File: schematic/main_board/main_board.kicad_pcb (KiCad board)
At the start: 2 copper layers, 15 parts, among them J1 Line OUT, J2 Line IN, P1 +Vref, P2 GND, P3 -Vref, P4 Probe, P5 GND, U1 LM324N

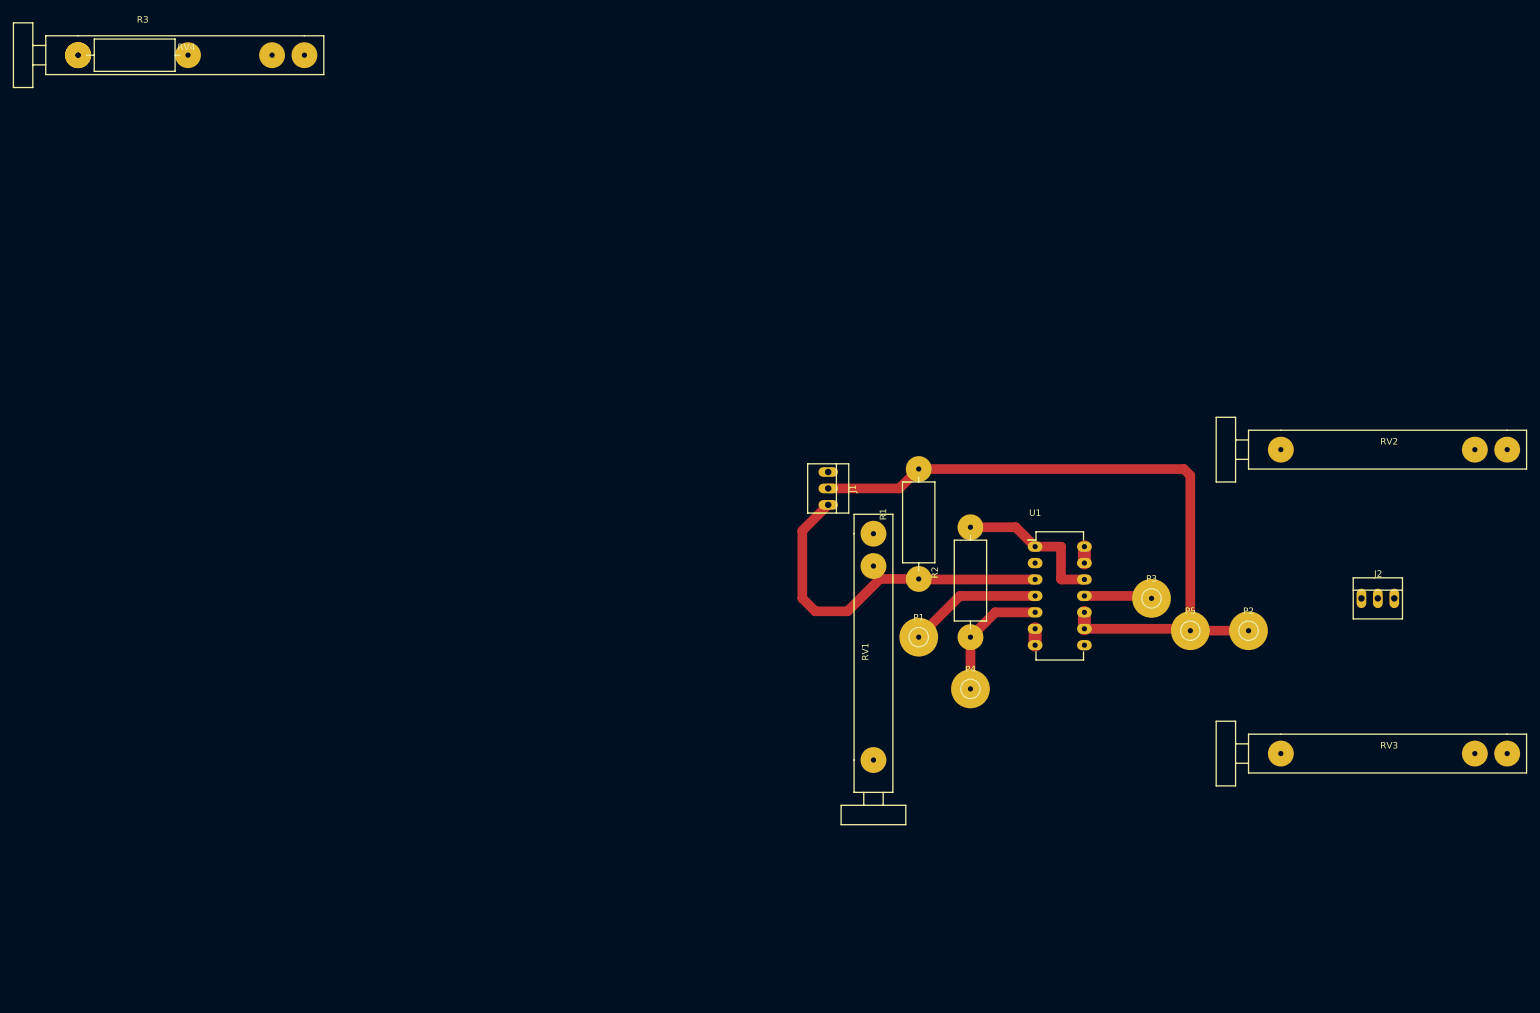
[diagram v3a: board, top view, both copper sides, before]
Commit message: Added footprints for some soviet elements which used on Main board.
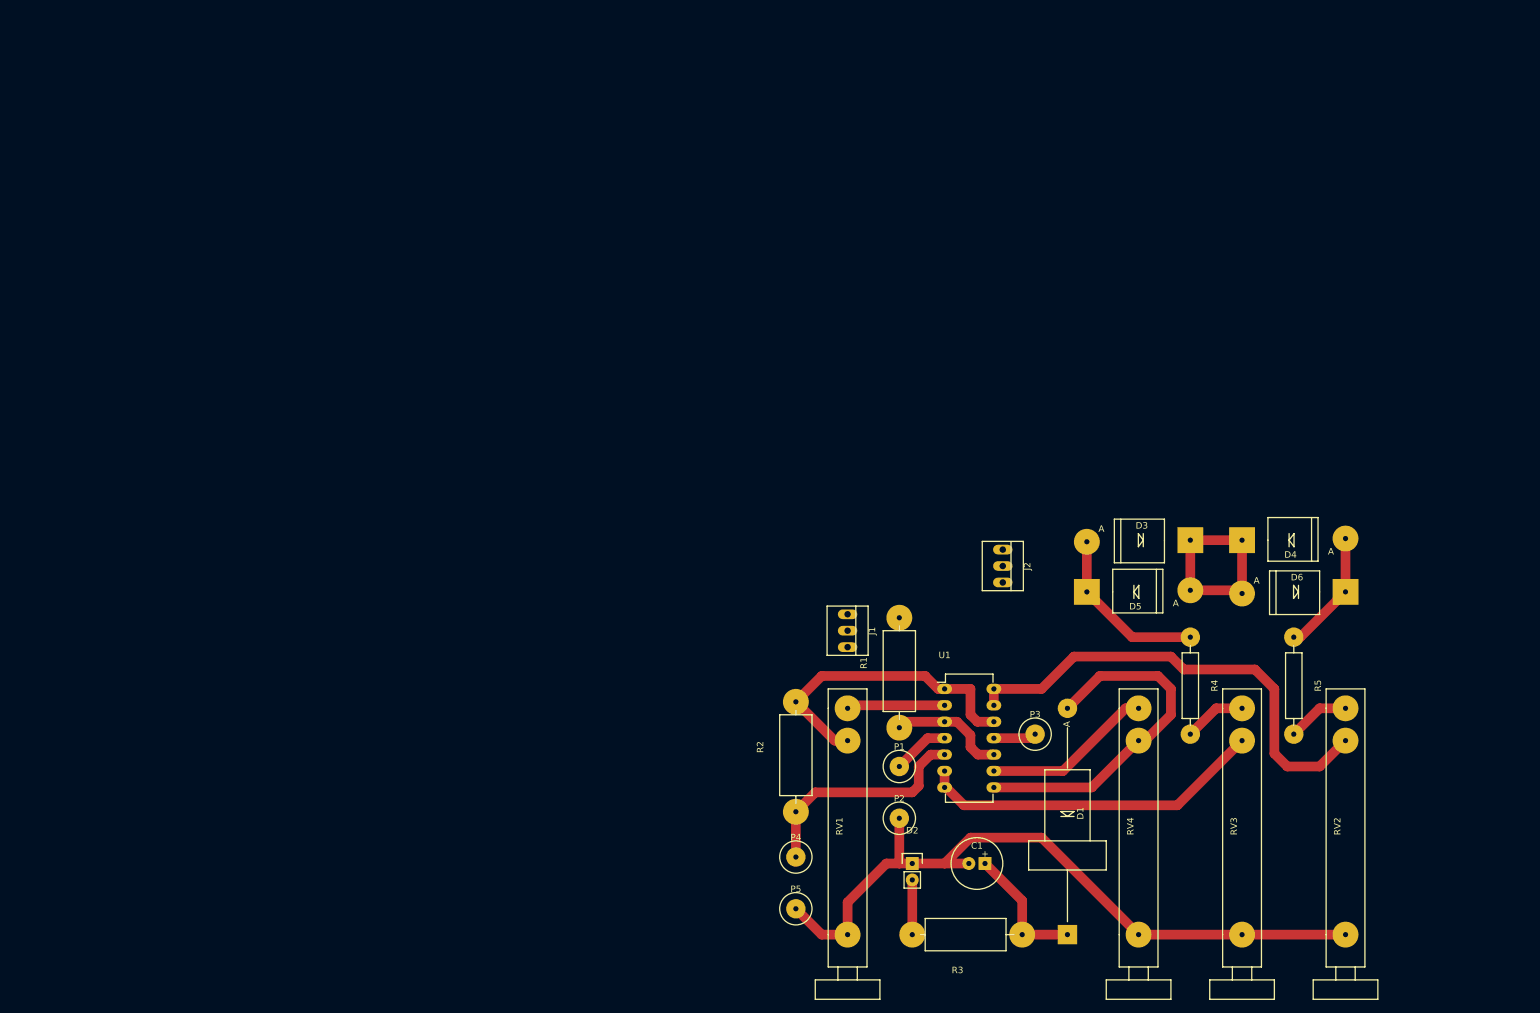
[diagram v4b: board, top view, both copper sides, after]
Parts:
- added C1: 100u, footprints:C100u_vert, F.Cu at (139.0, 125.0)
- added D1: D226, footprints:Diode_D226, F.Cu at (153.0, 136.0)
- added D2: LED, footprints:Pin_vert_1x02, F.Cu at (129.0, 125.0)
- added D3: KD105, footprints:Diode_KD105, F.Cu at (172.0, 75.0)
- added D4: KD105, footprints:Diode_KD105, F.Cu at (180.0, 75.0)
- added D5: KD105, footprints:Diode_KD105, F.Cu at (156.0, 83.0)
- added D6: KD105, footprints:Diode_KD105, F.Cu at (196.0, 83.0)
- added R4: 1k, footprints:Resistor_Horizontal_RM15mm, F.Cu at (172.0, 90.0)
- added R5: 1k, footprints:Resistor_Horizontal_RM15mm, F.Cu at (188.0, 90.0)
- J1: value Line OUT -> To Line OUT
- J2: value Line IN -> To Line IN
- P1, P2, P3, P4, P5: footprint footprints:1pin_big -> footprints:1pin_small
- moved RV4 213.1 mm to (164.0, 136.0), turned to 90 degrees
- moved R3 199.5 mm to (146.0, 136.0), turned to 180 degrees
- moved RV2 75.7 mm to (196.0, 136.0), turned to 90 degrees
- moved P5 74.6 mm to (111.0, 132.0)
- moved P2 61.3 mm to (127.0, 118.0)
- moved J2 58.2 mm to (143.0, 79.0), turned to 270 degrees
- moved R2 38.2 mm to (111.0, 117.0)
- moved P4 37.5 mm to (111.0, 124.0)
- moved RV3 28.6 mm to (180.0, 136.0), turned to 90 degrees
- moved P3 27.7 mm to (148.0, 105.0)
- moved RV1 27.3 mm to (119.0, 136.0)
- moved U1 26.1 mm to (134.0, 98.0)
- moved R1 23.2 mm to (127.0, 104.0)
- moved J1 22.2 mm to (119.0, 89.0)
- moved P1 20.2 mm to (127.0, 110.0)
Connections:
- J2 pad 1: Net-(J2-Pad1) -> Net-(D4-Pad2)
- J2 pad 3: Net-(J2-Pad3) -> Net-(D3-Pad2)
- RV2 pad 2: Net-(J2-Pad1) -> Net-(R5-Pad2)
- RV3 pad 2: Net-(J2-Pad3) -> Net-(R4-Pad2)
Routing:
- net Net-(RV2-Pad3): track 2.54 -> 73.5 mm
- net Net-(D1-Pad2): track 0.00 -> 54.9 mm
- net GND: track 91.1 -> 144.0 mm
- net Net-(RV3-Pad3): track 2.54 -> 53.8 mm
- net Net-(J1-Pad3): track 57.6 -> 18.2 mm
- net Net-(D3-Pad2): track 0.00 -> 26.6 mm
- net Net-(R2-Pad2): track 23.9 -> 48.0 mm
- net Net-(C1-Pad1): track 0.00 -> 20.4 mm
- net Net-(D4-Pad2): track 0.00 -> 19.1 mm
- net Net-(P4-Pad1): track 19.6 -> 35.4 mm
- net Net-(RV1-Pad2): track 0.00 -> 15.2 mm
- net +12V: track 20.6 -> 8.81 mm
- net Net-(RV4-Pad2): track 16.1 -> 26.4 mm
- net Net-(R5-Pad2): track 0.00 -> 9.66 mm
- net Net-(R4-Pad2): track 0.00 -> 9.66 mm
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
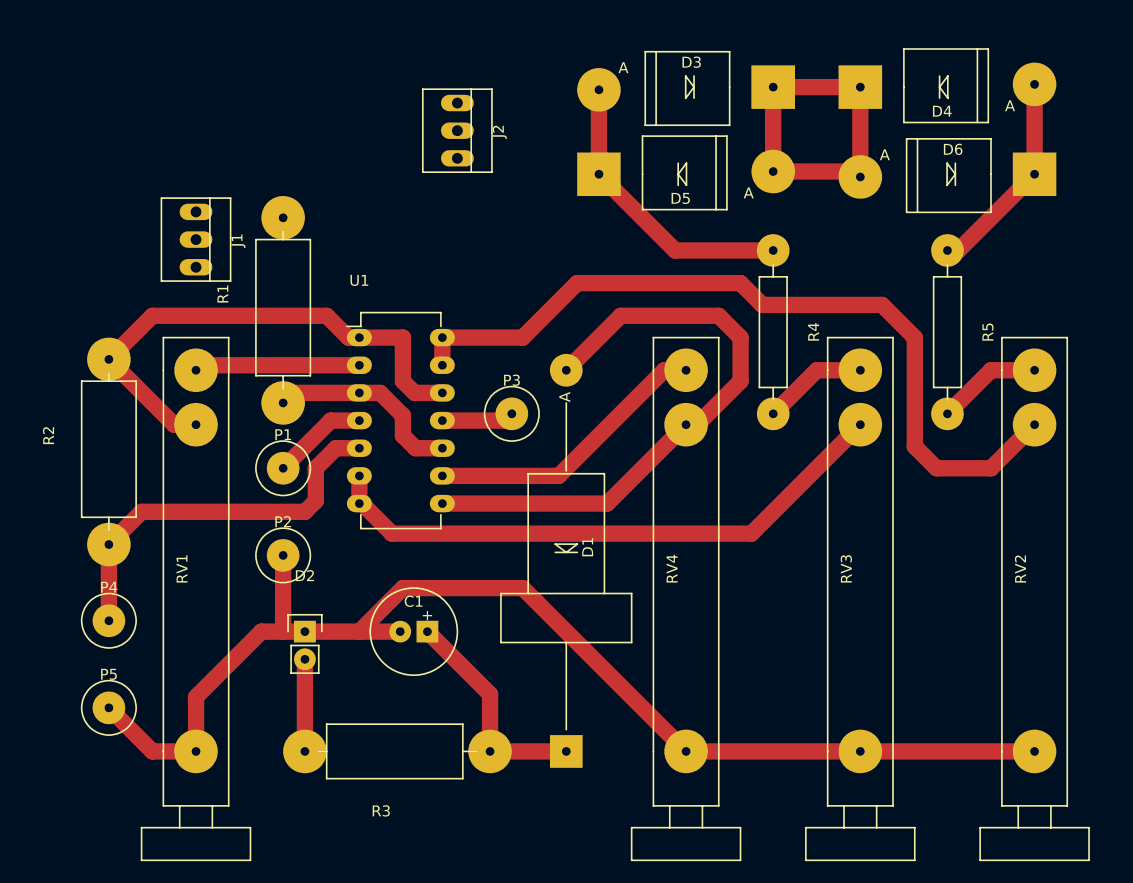
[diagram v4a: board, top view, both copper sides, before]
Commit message: Added 0.1u capacitors and filled zones to PCB.
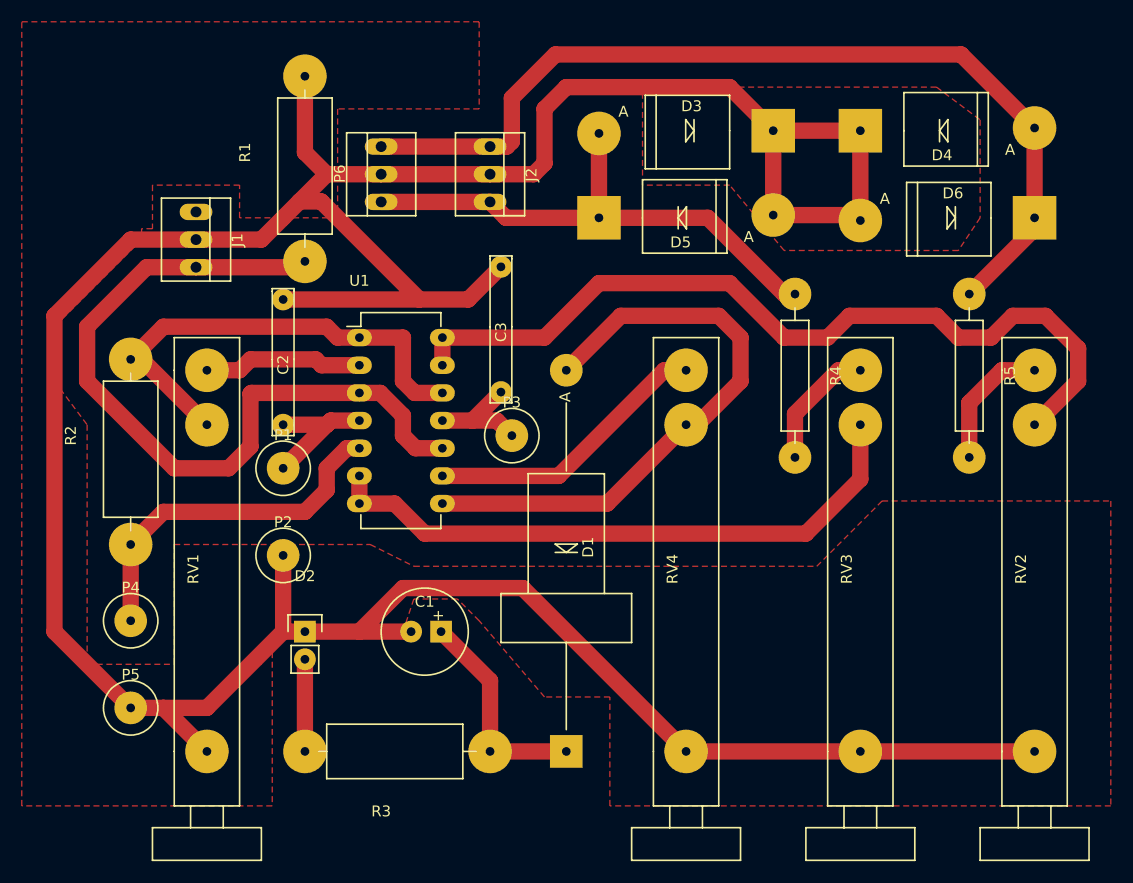
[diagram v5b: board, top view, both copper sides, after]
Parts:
- added C2: 0.1u, footprints:C_0.1u, F.Cu at (127.0, 106.0)
- added C3: 0.1u, footprints:C_0.1u, F.Cu at (147.0, 103.0)
- added P6: Calibration, Connect:PINHEAD1-3, F.Cu at (136.0, 83.0)
- moved R1 13.2 mm to (129.0, 91.0)
- moved J2 5.00 mm to (146.0, 83.0)
- moved R4 4.47 mm to (174.0, 94.0)
- moved R5 4.47 mm to (190.0, 94.0)
- moved D3 4.00 mm to (172.0, 79.0)
- moved D4 4.00 mm to (180.0, 79.0)
- moved D5 4.00 mm to (156.0, 87.0)
- moved D6 4.00 mm to (196.0, 87.0)
- moved P3 2.00 mm to (148.0, 107.0)
- moved P4 2.00 mm to (113.0, 124.0)
- moved P5 2.00 mm to (113.0, 132.0)
- moved R2 2.00 mm to (113.0, 117.0)
- moved C1 1.00 mm to (140.0, 125.0)
- moved RV1 1.00 mm to (120.0, 136.0)
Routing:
- net GND: track 144.0 -> 306.4 mm
- net Net-(D4-Pad2): track 19.1 -> 86.4 mm
- net Net-(J1-Pad3): track 18.2 -> 72.3 mm
- net Net-(D3-Pad2): track 26.6 -> 49.3 mm
- net +12V: track 8.81 -> 13.4 mm
- net -12V: track 6.64 -> 10.7 mm
- net Net-(RV2-Pad3): track 73.5 -> 77.4 mm
- net Net-(R2-Pad2): track 48.0 -> 44.2 mm
- net Net-(RV3-Pad3): track 53.8 -> 57.0 mm
- net Net-(R5-Pad2): track 9.66 -> 12.2 mm
- net Net-(P4-Pad1): track 35.4 -> 32.8 mm
- net Net-(R4-Pad2): track 9.66 -> 11.7 mm
- net Net-(C1-Pad1): track 20.4 -> 19.9 mm
- added copper zone on F.Cu, net GND
